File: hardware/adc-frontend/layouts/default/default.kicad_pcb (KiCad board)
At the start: 2 copper layers, 113 parts

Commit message: 基板初期配置(機能ブロック別)+ 外形120x90を追加
全107フットプリントを機能ブロックごとに配置した初期案:
- 左辺: D-SUB15(映像入力)、2x8ボックスヘッダ(ArgusX代替入力)、YSテストパッド
- 中央: TVP7002 + デカップリング/PLLフィルタ/制御R/27MHz OSC
- その左: アナログ前段(ESD/75Ω終端/ACカップリング)、同期バッファ
- 上辺: 電源(USB-C/DCジャック/LDO×4/バルク) + 音声(PCM1808×2/XO/3.5mm/TOSLINK)
- 右辺: MagJack×2 + MAC EEPROM×2 + GbEキャップ
- 下辺: スタッキングヘッダ P2/P4/P1(EXT基板と嵌合、位置は採寸で要調整)
基板外形120x90mmは仮(EXT基板実寸で確定)。ato build全ターゲット成功、
再ビルドで配置保持を確認。★DRC/重なり解消・配線・EXT採寸整合は次工程。

Co-Authored-By: Claude Fable 5 <noreply@anthropic.com>
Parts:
- removed C45, C46, C63, C64, C65, C66: {ℝ+}F, SAMSUNG_CL05B104KO5NNNC:C0402
- moved C42 937.8 mm to (92.5, 24.5)
- moved C41 932.3 mm to (88.0, 24.5)
- moved C44 897.7 mm to (92.5, 20.0)
- moved C43 892.2 mm to (88.0, 20.0)
- moved J5 866.8 mm to (46.0, 70.0)
- moved J2 866.5 mm to (104.0, 30.0), turned to 270 degrees
- moved J1 863.9 mm to (100.0, 82.0)
- moved C40 862.4 mm to (89.0, 49.0)
- moved C39 857.4 mm to (84.0, 49.0)
- moved U5 842.2 mm to (89.0, 44.0)
- moved U4 837.2 mm to (84.0, 44.0)
- moved C19 816.2 mm to (84.0, 16.0)
- moved D1 808.4 mm to (72.0, 26.0)
- moved J8 802.0 mm to (88.0, 8.00)
- moved J6 800.0 mm to (70.0, 6.00)
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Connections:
- J11 pad 11: ct_caps[7]-power-hv -> eth.jack2-led_g_a
- J11 pad 12: eth1_4n -> eth.jack2-led_g_k
- J11 pad 13: eth.jack2-led_g_a -> eth.jack2-led_y_k
- J11 pad 14: eth.jack2-led_g_k -> eth.jack2-led_y_a
- J11 pad P1: (no net) -> ct_caps[1]-power-hv
- J11 pad P10: (no net) -> chassis
- J11 pad P2: (no net) -> eth1_1p
- J11 pad P3: (no net) -> eth1_1n
- J11 pad P4: (no net) -> eth1_2p
- J11 pad P5: (no net) -> eth1_3p
- J11 pad P6: (no net) -> eth1_3n
- J11 pad P7: (no net) -> eth1_2n
- J11 pad P8: (no net) -> eth1_4p
- J11 pad P9: (no net) -> eth1_4n
- J11 pad SHIELD0: (no net) -> chassis
- J11 pad SHIELD1: (no net) -> chassis
- J2 pad 11: ct_caps[3]-power-hv -> led_g_a
- J2 pad 12: eth2_4n -> led_g_k
- J2 pad 13: led_g_a -> led_y_k
- J2 pad 14: led_g_k -> led_y_a
- J2 pad P1: (no net) -> ct_caps[0]-power-hv
- J2 pad P10: (no net) -> chassis
- J2 pad P2: (no net) -> eth2_1p
- J2 pad P3: (no net) -> eth2_1n
- J2 pad P4: (no net) -> eth2_2p
- J2 pad P5: (no net) -> eth2_3p
- J2 pad P6: (no net) -> eth2_3n
- J2 pad P7: (no net) -> eth2_2n
- J2 pad P8: (no net) -> eth2_4p
- J2 pad P9: (no net) -> eth2_4n
- J2 pad SHIELD0: (no net) -> chassis
- J2 pad SHIELD1: (no net) -> chassis
- J6 pad 1: c_in_l-power-hv-1 -> gnd
- J6 pad 2: c_in_r-power-hv-1 -> c_in_l-power-hv-1
- J6 pad 3: gnd -> jack_line-switch
- J6 pad 4: tip_sw -> c_in_r-power-hv-1
- J9 pad 2: power_5v-hv -> gnd
- J9 pad 3: (no net) -> gnd
- J9 pad 4: (no net) -> gnd
- J9 pad A1B12: (no net) -> gnd
- J9 pad A4B9: (no net) -> power_5v-hv
- J9 pad A5: (no net) -> A5
- J9 pad A6: (no net) -> dp
- J9 pad A7: (no net) -> dn
- J9 pad A8: (no net) -> A8
- J9 pad B1A12: (no net) -> gnd
- J9 pad B4A9: (no net) -> power_5v-hv
- J9 pad B5: (no net) -> B5
- J9 pad B6: (no net) -> dp
- J9 pad B7: (no net) -> dn
- J9 pad B8: (no net) -> B8
- R4 pad 1: 5-1 -> A5
- R5 pad 1: 12 -> B5
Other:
- board outline added: 120 x 90 mm

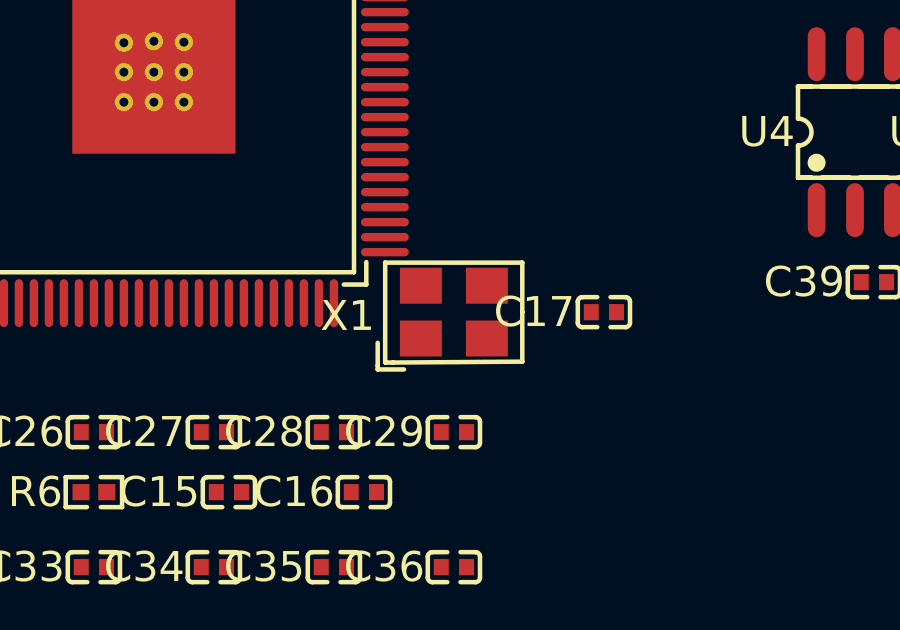
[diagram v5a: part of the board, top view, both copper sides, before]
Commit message: 27MHz EXT_CLKを水晶→アクティブ発振器へ修正(部品選定ミス修正)
Osc27Mが4ピン発振器配線(VCC/GND/OUT/EN)なのに、選定部品が水晶(C9008
X322527MSB4SI)だった不整合を修正。TVP7002 EXT_CLKは単線クロック入力なので
アクティブ発振器で駆動するのが正。YXC OT322527MJBA4SL(C725995、OSC-SMD_4P、
3.3V CMOS、pin1=Tri-state/2=GND/3=OUT/4=VDD)へ差し替え。配線は不変。
旧水晶partは削除。ato build全ターゲット成功、BOMにX1=OT322527MJBA4SL確認。

Co-Authored-By: Claude Fable 5 <noreply@anthropic.com>
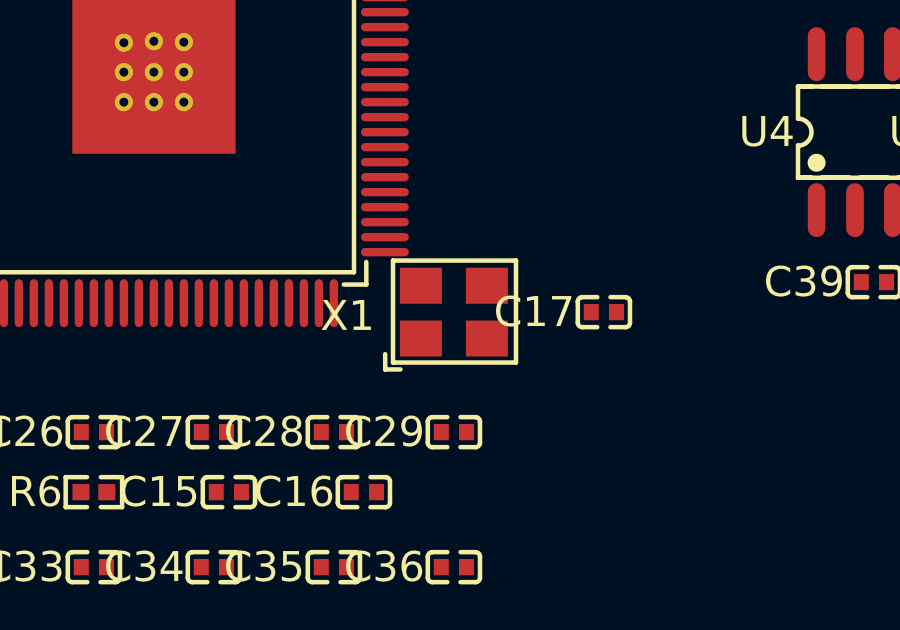
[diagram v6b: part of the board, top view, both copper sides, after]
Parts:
- X1: footprint YXC_X322527MSB4SI:CRYSTAL-SMD_4P-L3.2-W2.5-BL-1 -> YXC_OT322527MJBA4SL:OSC-SMD_4P-L3.2-W2.5-BL
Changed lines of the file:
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@@
 		)
 	)
-	(footprint "YXC_X322527MSB4SI:CRYSTAL-SMD_4P-L3.2-W2.5-BL-1"
+	(footprint "YXC_OT322527MJBA4SL:OSC-SMD_4P-L3.2-W2.5-BL"
 		(layer "F.Cu")
 		(at 70 50 0)
@@
 			)
 		)
-		(property "LCSC" "C9008"
+		(property "LCSC" "C725995"
 			(at 0 0 0)
 			(layer "User.9")
@@
 			(hide yes)
 		)
-		(property "Partnumber" "X322527MSB4SI"
+		(property "Partnumber" "OT322527MJBA4SL"
 			(at 0 0 0)
 			(layer "User.9")
@@
 			(hide yes)
 		)
-		(property "lcsc_id" "C9008"
+		(property "lcsc_id" "C725995"
 			(at 0 0 0)
 			(layer "User.9")
@@
 		(attr smd)
 		(fp_line
-			(start -2.54 1.02)
-			(end -2.54 1.78)
-			(stroke
-				(width 0.15)
-				(type solid)
-			)
-			(layer "F.SilkS")
-			(layers "F.SilkS")
-			(locked no)
-		)
-		(fp_line
-			(start -2.54 1.78)
-			(end -2.54 1.91)
+			(start -2.03 -1.72)
+			(end -2.03 1.68)
 			(stroke
 				(width 0.15)
@@
 		(fp_line
 			(start -2.03 1.68)
-			(end -2.29 1.68)
+			(end 2.07 1.68)
 			(stroke
 				(width 0.15)
@@
 		)
 		(fp_line
-			(start -2.29 1.68)
-			(end -2.29 -1.65)
+			(start 2.07 1.68)
+			(end 2.07 -1.72)
 			(stroke
 				(width 0.15)
@@
 		)
 		(fp_line
-			(start -2.29 -1.65)
-			(end 2.28 -1.65)
+			(start 2.07 -1.72)
+			(end -2.03 -1.72)
 			(stroke
 				(width 0.15)
@@
 		)
 		(fp_line
-			(start 2.28 -1.65)
-			(end 2.28 -0)
+			(start -2.29 1.4)
+			(end -2.29 1.91)
 			(stroke
 				(width 0.15)
@@
 		)
 		(fp_line
-			(start 2.28 -0)
-			(end 2.28 1.65)
-			(stroke
-				(width 0.15)
-				(type solid)
-			)
-			(layer "F.SilkS")
-			(layers "F.SilkS")
-			(locked no)
-		)
-		(fp_line
-			(start 2.28 1.65)
-			(end -2.03 1.68)
-			(stroke
-				(width 0.15)
-				(type solid)
-			)
-			(layer "F.SilkS")
-			(layers "F.SilkS")
-			(locked no)
-		)
-		(fp_line
-			(start -2.54 1.91)
-			(end -1.66 1.91)
+			(start -2.29 1.91)
+			(end -1.78 1.91)
 			(stroke
 				(width 0.15)
@@
 		)
 		(fp_circle
-			(center -1.4 0.89)
-			(end -1.15 0.89)
+			(center -1.09 1.57)
+			(end -0.96 1.57)
 			(stroke
-				(width 0.5)
+				(width 0.25)
 				(type solid)
 			)
@@
 		)
 		(embedded_fonts no)
-		(model "${KIPRJMOD}/../../parts/YXC_X322527MSB4SI/CRYSTAL-SMD_4P-L3.2-W2.5-BL-1.step"
+		(model "${KIPRJMOD}/../../parts/YXC_OT322527MJBA4SL/OSC-SMD_4P-L3.2-W2.5-CJ13-320001210A20.step"
 			(offset
 				(xyz 0 0 -0)
